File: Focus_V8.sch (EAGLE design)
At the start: 100 parts, among them X1 USB+SHIELD, Y1 16Mhz

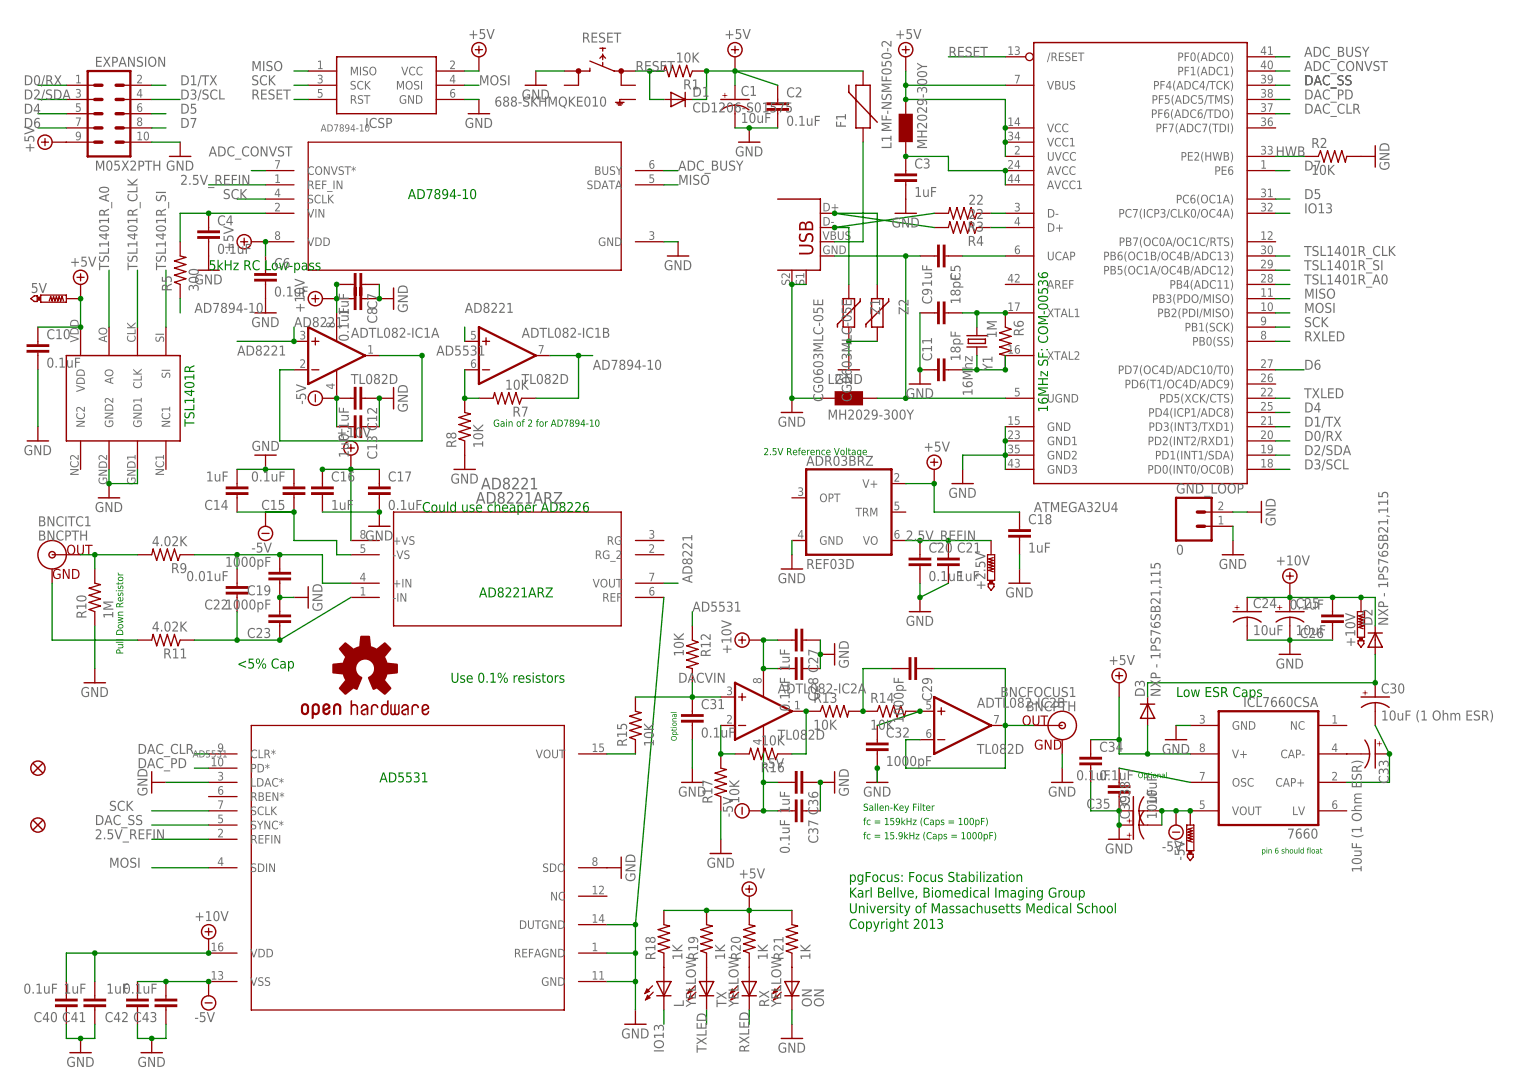
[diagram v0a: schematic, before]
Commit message: Version 8 removes the Linear Light Array and uses a TSL1401CL-Adapter Board via a 5 pin JST SH connector. There is also a 3 pin JST connector for communicating with a Serial Enabled LCD display RGB LED has also been added to give a status indication.
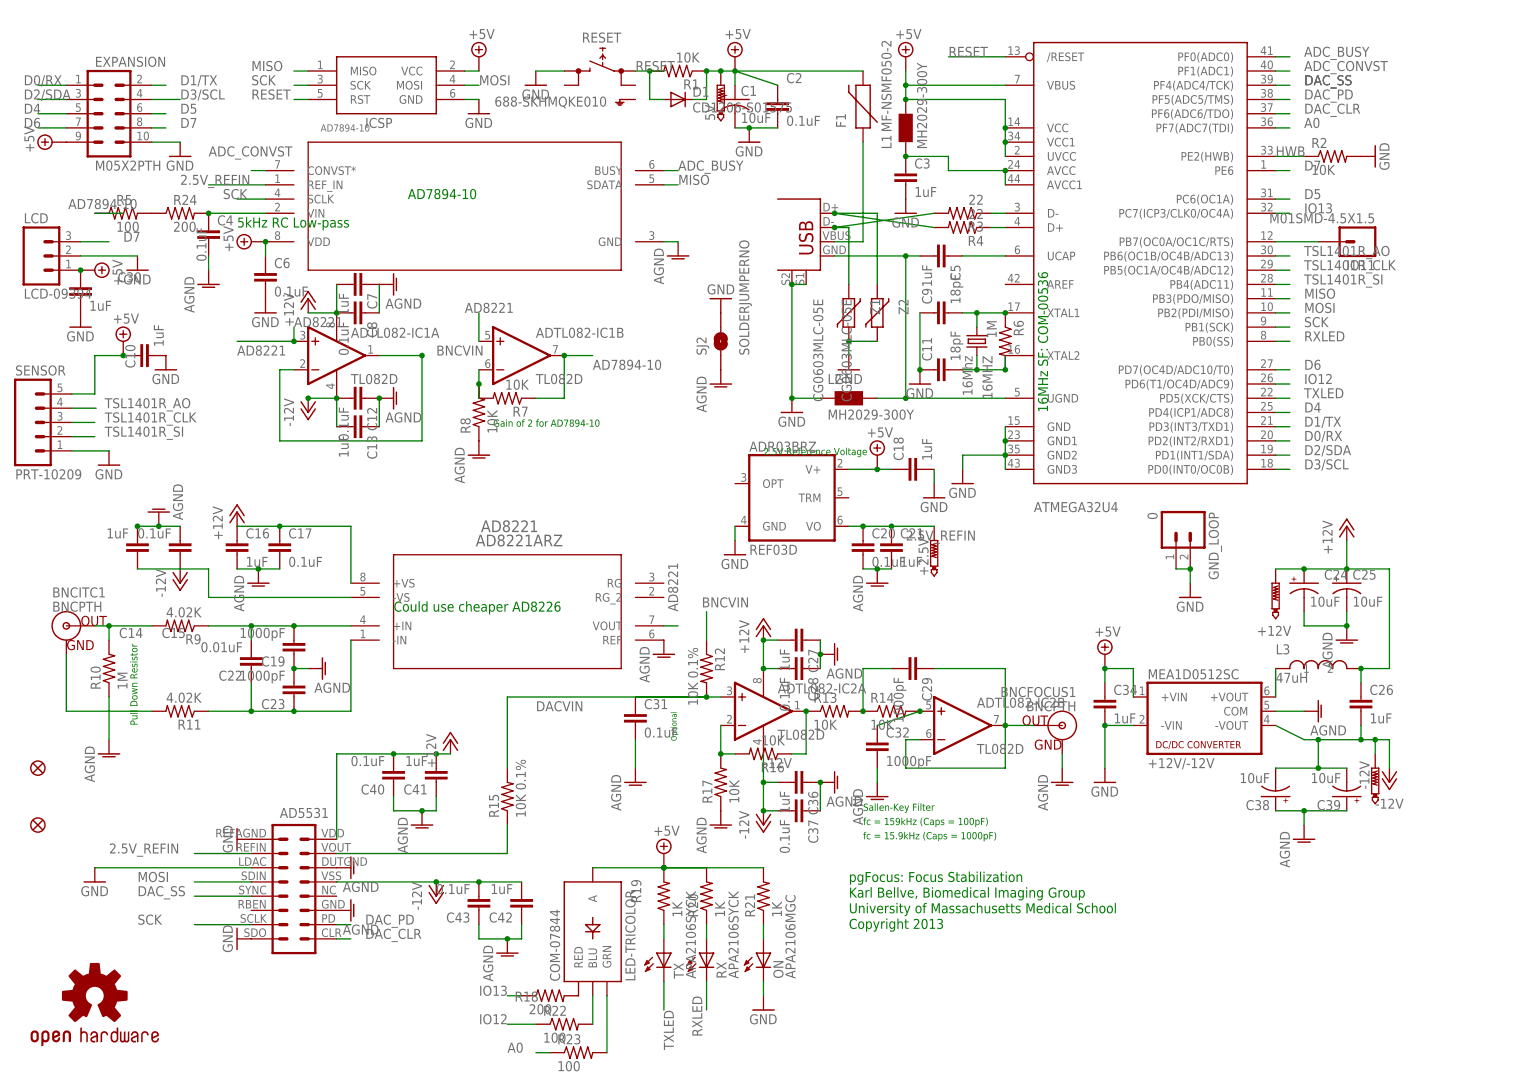
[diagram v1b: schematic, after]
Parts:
- removed +10V, -5V: PTR1TP20R, testpad:PTR1TP20R
- removed 7660: ICL7660CSA, maxim:ICL7660CSA
- removed AD5531: AD5531BRUZ, BIG:AD5531BRUZ
- removed C33: 10uF (1 Ohm ESR), SparkFun:CAP_POL1206-KIT
- removed C35: 0.1uF, SparkFun:CAP0603-CAP
- removed D2, D3: NXP - 1PS76SB21,115, SparkFun:DIODESOD
- removed L: YELLOW, BIG:LEDCHIPLED_0805
- added +12V, -12V: PTR1TP20R, testpad:PTR1TP20R
- added COM-07844: LED-TRICOLOR, SparkFun-LED:LED-TRICOLOR
- added IO11: M01SMD-4.5X1.5, SparkFun-Connectors:M01SMD-4.5X1.5
- added L3: 47uH, BIG:11R473C
- added LCD: LCD-09394, SparkFun-Connectors:M03JST-PTH
- added MEA1D0512SC: +12V/-12V, dc-dc-converter:NMA
- added R22, R23: 100, SparkFun:RESISTOR0603-RES
- added R24: 200, SparkFun:RESISTOR0603-RES
- added SENSOR: PRT-10209, SparkFun-Connectors:M05SMD2
- added SJ2: SOLDERJUMPERNO, SparkFun-Passives:SOLDERJUMPERNO
- C10, C26, C34: value 0.1uF -> 1uF
- C30: value 10uF (1 Ohm ESR) -> 1uF; device SparkFun:CAP_POL1206-KIT -> SparkFun:CAP0603-CAP
- ON: value ON -> APA2106MGC
- R12, R15: value 10K -> 10K 0.1%
- R18: value 1K -> 200
- R5: value 300 -> 100
- RX, TX: value YELLOW -> APA2106SYCK
- U$1: value TSL1401CL -> AD5331; device BIG:TSL1401CL -> BIG:AD5331
- renumbered Y1 to 16MHZ
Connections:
- net AD5531 renamed BNCVIN
- removed net +10V: +10V.TP, AD5531.VDD, AD8221.+VS, ADTL082-IC1P.V+, ADTL082-IC2P.V+, C16.1, C17.1, C24.+, C25.+, C26.2, C27.2, C28.2, C40.2, C41.2, C7.2, C8.2, D2.C
- removed net -5V: -5V.TP, 7660.VOUT, AD5531.VSS, AD8221.-VS, ADTL082-IC1P.V-, ADTL082-IC2P.V-, C12.2, C13.2, C14.1, C15.1, C36.2, C37.2, C38.-, C39.-, C42.2, C43.2
- removed net N$27: L.A, R18.1
- removed net TSL1401R_A0: ATMEGA32U4.PB4(ADC11), U$1.AO
- new net +12V: +12V.TP, AD8221.+VS, ADTL082-IC1P.V+, ADTL082-IC2P.V+, C16.1, C17.1, C24.+, C25.+, C26.1, C27.2, C28.2, C40.2, C41.2, C7.2, C8.2, L3.2, U$1.VDD
- new net -12V: -12V.TP, AD8221.-VS, ADTL082-IC1P.V-, ADTL082-IC2P.V-, C12.2, C13.2, C14.1, C15.1, C26.2, C36.2, C37.2, C38.-, C39.-, C42.2, C43.2, MEA1D0512SC.-VOUT, U$1.VSS
- new net A0: ATMEGA32U4.PF7(ADC7(TDI), R23.1
- new net AGND: AD7894-10.GND, AD8221.REF, BNCFOCUS1.GND, C12.1, C13.1, C14.2, C15.2, C16.2, C17.2, C19.1, C20.2, C21.2, C23.2, C24.-, C25.-, C27.1, C28.1, C31.2, C32.2, C36.1, C37.1, C38.+, C39.+, C4.2, C40.1, C41.1, C42.1, C43.1, C7.1, C8.1, MEA1D0512SC.COM, R10.1, R17.1, R8.1, SJ2.1, U$1.DUTGND, U$1.GND
- new net IO12: ATMEGA32U4.PD6(T1/OC4D/ADC9), R22.1
- new net N$29: COM-07844.RED, R18.2
- new net N$6: L3.1, MEA1D0512SC.+VOUT
- new net TSL1401R_AO: ATMEGA32U4.PB6(OC1B/OC4B/ADC13), SENSOR.4
- net +5V: now also C30.1, COM-07844.A, LCD.1, MEA1D0512SC.+VIN, SENSOR.5; no longer 7660.V+, D3.A, R18.2, U$1.VDD
- net 2.5V_REFIN: now also U$1.REFIN; no longer AD5531.REFIN
- net D7: now also LCD.3
- net DAC_CLR: now also U$1.CLR; no longer AD5531.CLR*
- net DAC_PD: now also U$1.PD; no longer AD5531.PD*
- net DAC_SS: now also U$1.SYNC; no longer AD5531.SYNC*
- net GND: now also C30.2, LCD.2, MEA1D0512SC.-VIN, SENSOR.1, SJ2.2, U$1.LDAC, U$1.REFAGND, U$1.SDO; no longer 7660.GND, AD5531.DUTGND, AD5531.GND, AD5531.LDAC*, AD5531.REFAGND, AD5531.SDO, AD7894-10.GND, AD8221.REF, BNCFOCUS1.GND, C12.1, C13.1, C14.2, C15.2, C16.2, C17.2, C19.1, C20.2, C21.2, C23.2, C24.-, C25.-, C26.1, C27.1, C28.1, C31.2, C32.2, C35.1, C36.1, C37.1, C38.+, C39.+, C4.2, C40.1, C41.1, C42.1, C43.1, C7.1, C8.1, R10.1, R17.1, R8.1, U$1.GND1, U$1.GND2
- net IO13: now also R18.1; no longer L.C
- net MOSI: now also U$1.SDIN; no longer AD5531.SDIN
- net N$28: now also ATMEGA32U4.PB7(OC0A/OC1C/RTS), IO11.1; no longer C30.+, D2.A, D3.C
- net N$3: now also R24.2; no longer R5.2
- net N$30: now also COM-07844.BLU, R22.2; no longer 7660.CAP-, C33.-
- net N$31: now also COM-07844.GRN, R23.2; no longer 7660.CAP+, C30.-, C33.+
- net N$5: now also R24.1, R5.2; no longer 7660.OSC, C35.2
- net N$8: now also U$1.VOUT; no longer AD5531.VOUT
- net SCK: now also U$1.SCLK; no longer AD5531.SCLK
- net TSL1401R_CLK: now also ATMEGA32U4.PB5(OC1A/OC4B/ADC12), SENSOR.3; no longer ATMEGA32U4.PB6(OC1B/OC4B/ADC13), U$1.CLK
- net TSL1401R_SI: now also ATMEGA32U4.PB4(ADC11), SENSOR.2; no longer ATMEGA32U4.PB5(OC1A/OC4B/ADC12), U$1.SI
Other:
- note removed: "<5% Cap"
- note removed: "AD5531"
- note removed: "AD8221ARZ"
- note removed: "Low ESR Caps"
- note removed: "TSL1401R"
- note removed: "Use 0.1% resistors"
- note removed: "pin 6 should float"
- moved on the sheet: +2.5V, 5V, AD8221, ADR03BRZ, ADTL082-IC1B, BNCITC1, C10, C14, C15, C16, C17, C18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
